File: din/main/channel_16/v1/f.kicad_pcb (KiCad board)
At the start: 2 copper layers, 76.8 x 81.3 mm, 77 parts, among them J1 fm16_i, J2 wrs_i, J3 wrs_i, J4 bus_i, J5 selector4_i, U1 LTV-357T, U10 LTV-357T, U11 LTV-357T, U12 LTV-357T, U13 LTV-357T, U15 LTV-357T, U16 LTV-357T, U17 LTV-357T, U18 LTV-357T, U2 LTV-357T, U21 74LS245, U22 74LS245, U3 LTV-357T, U4 LTV-357T, U6 LTV-357T, U7 LTV-357T, U8 LTV-357T, U9 LTV-357T

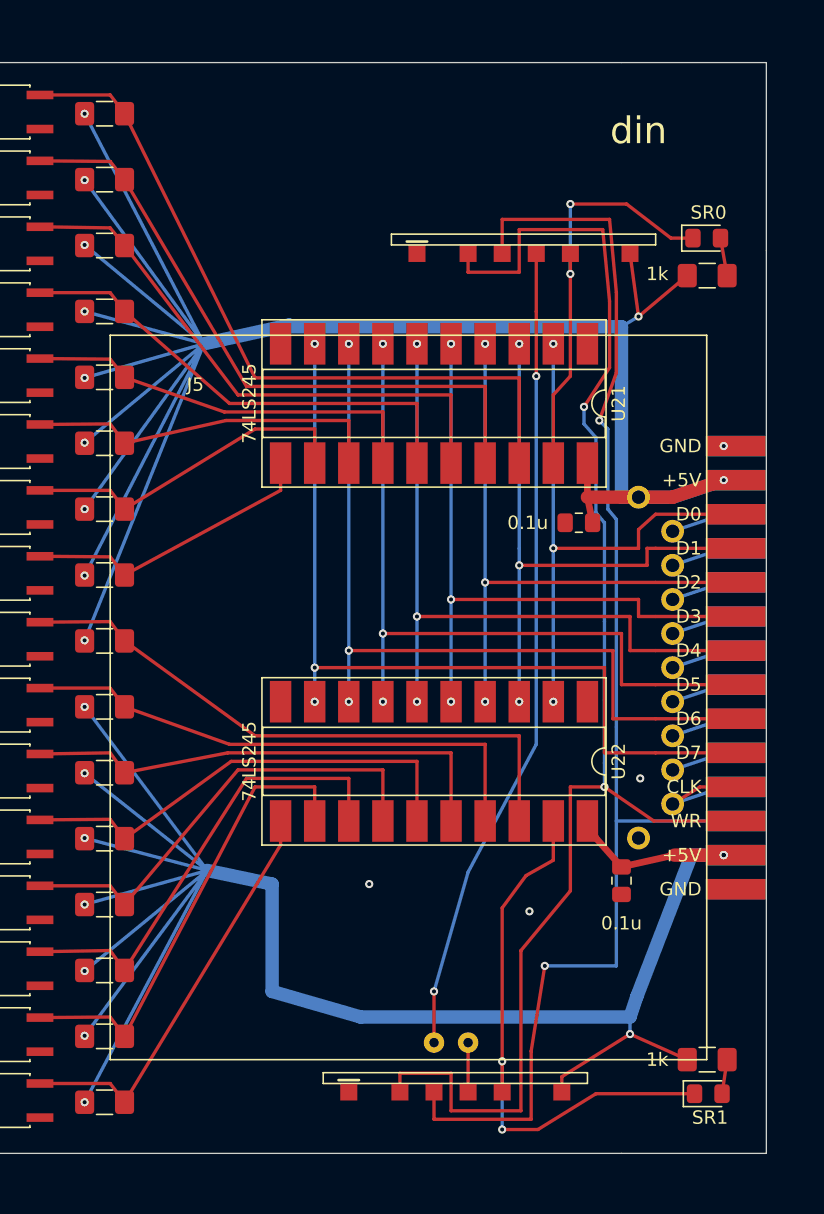
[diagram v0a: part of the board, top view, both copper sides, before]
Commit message: voltage regulator for each module
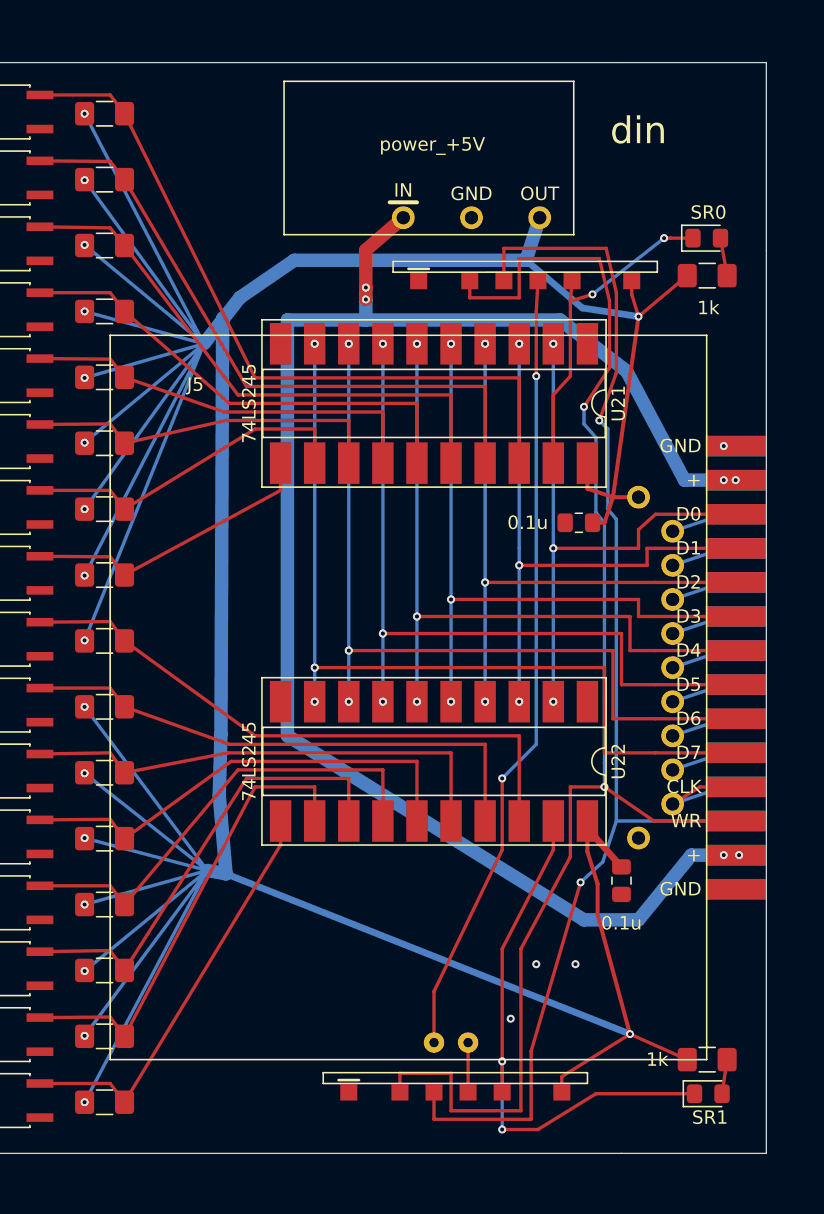
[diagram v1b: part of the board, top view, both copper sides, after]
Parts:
- added J6: power_+5V, plc88:power_i, F.Cu at (77.7, 31.9)
- J4: footprint 1my_elements:Bus88_2x14 -> plc88:bus_im
- moved J2 2.04 mm to (92.2, 44.2)
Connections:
- J4 pad 25: +5V -> VPBUS
- J4 pad 26: +5V -> VPBUS
- J4 pad 3: +5V -> VPBUS
- J4 pad 4: +5V -> VPBUS
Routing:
- net VPBUS: track 0.00 -> 119.1 mm, vias 0 -> 6
- net +5V: track 384.9 -> 404.0 mm, vias 21 -> 18
- net RD: track 101.9 -> 95.3 mm
- net SR0: track 31.3 -> 24.7 mm
- net WR: track 109.1 -> 105.8 mm
- net S0: track 60.4 -> 59.0 mm
- net SR1: track 42.3 -> 41.4 mm
